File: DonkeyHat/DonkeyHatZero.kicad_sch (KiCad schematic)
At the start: 17 parts, among them J1 GPIO, J2 Encoder 2, J3 Encoder 1, J4 I2C, J5 Battery +, J6 Battery -, J7 +5v, J8 GND, U2 rp2040-zero

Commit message: Zero WIP
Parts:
- removed 5V1: Conn_01x02_Pin, Connector_PinHeader_2.54mm:PinHeader_1x02_P2.54mm_Vertical, symbol Connector:Conn_01x02_Pin
- removed I2C1, OLED1: Conn_01x04_Pin, Connector_PinHeader_2.54mm:PinHeader_1x04_P2.54mm_Vertical, symbol Connector:Conn_01x04_Pin
- removed J2: Encoder 2, Connector_PinHeader_2.54mm:PinHeader_1x04_P2.54mm_Vertical, symbol Connector:Conn_01x04_Pin
- removed J3: Encoder 1, Connector_PinHeader_2.54mm:PinHeader_1x04_P2.54mm_Vertical, symbol Connector:Conn_01x04_Pin
- removed J4: I2C, Connector_JST:JST_SH_BM04B-SRSS-TB_1x04-1MP_P1.00mm_Vertical, symbol dk_Rectangular-Connectors-Headers-Male-Pins:B4B-PH-K-S_LF__SN_
- added J2, J3: Conn_01x02_Pin, Connector_PinHeader_2.54mm:PinHeader_1x02_P2.54mm_Vertical, symbol Connector:Conn_01x02_Pin
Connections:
- net GND: no longer J1.20 (Pin_20), J1.25 (Pin_25), J1.30 (Pin_30), J1.34 (Pin_34), J1.39 (Pin_39), J1.9 (Pin_9)
- net GPIO2/SDA1: no longer J1.3 (Pin_3)
- net GPIO3/SCL1: no longer J1.5 (Pin_5)
- net GPIO5: no longer J1.29 (Pin_29)
- net at J6.1 (Pin_1): now also J2.2 (Pin_2), J3.2 (Pin_2)
- net at J5.1 (Pin_1): now also J2.1 (Pin_1), J3.1 (Pin_1)
- net +3V3: no longer names the net of J1.1 (Pin_1)
- net +3V3: no longer J1.17 (Pin_17)
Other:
- moved on the sheet: J5, J6

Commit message: Ready for routing
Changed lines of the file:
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@@
 	(wire
 		(pts
-			(xy 121.92 29.21) (xy 133.35 29.21)
+			(xy 121.92 29.21) (xy 139.7 29.21)
 		)
 		(stroke
@@
 	(wire
 		(pts
-			(xy 133.35 29.21) (xy 133.35 43.18)
+			(xy 139.7 29.21) (xy 139.7 43.18)
 		)
 		(stroke
@@
 	(wire
 		(pts
-			(xy 116.84 43.18) (xy 133.35 43.18)
+			(xy 116.84 43.18) (xy 139.7 43.18)
 		)
 		(stroke
@@
 					(unit 1)
 				)
+			)
+		)
+	)
+	(symbol
+		(lib_id "power:GND")
+		(at 127 35.56 90)
+		(unit 1)
+		(exclude_from_sim no)
+		(in_bom yes)
+		(on_board yes)
+		(dnp no)
+		(property "Reference" "#PWR07"
+			(at 133.35 35.56 0)
+			(effects
+				(font
+					(size 1.27 1.27)
+				)
+				(hide yes)
+			)
+		)
+		(property "Value" "GND"
+			(at 131.3244 35.4457 0)
+			(effects
+				(font
+					(size 1.27 1.27)
+				)
+			)
+		)
+		(property "Footprint" ""
+			(at 127 35.56 0)
+			(effects
+				(font
+					(size 1.27 1.27)
+				)
+			)
+		)
+		(property "Datasheet" ""
+			(at 127 35.56 0)
+			(effects
+				(font
+					(size 1.27 1.27)
+				)
+			)
+		)
+		(property "Description" ""
+			(at 127 35.56 0)
+			(effects
+				(font
+					(size 1.27 1.27)
+				)
+				(hide yes)
+			)
+		)
+		(pin "1"
+		)
+		(instances
+			(project "DonkeyHatZero"
+				(path "/e63e39d7-6ac0-4ffd-8aa3-1841a4541b55"
+					(reference "#PWR07")
+					(unit 1)
+				)

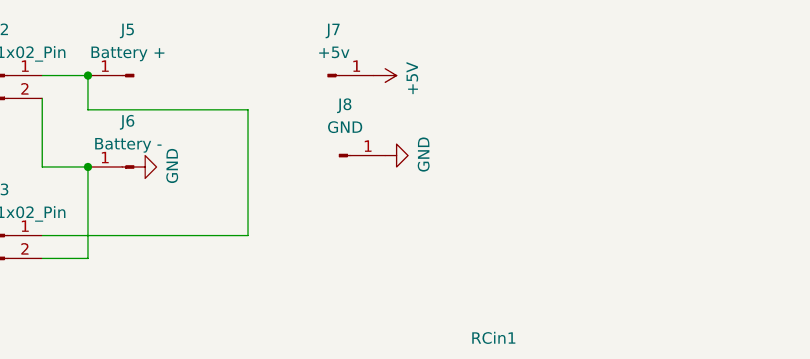
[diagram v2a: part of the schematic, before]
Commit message: Fixed spacing
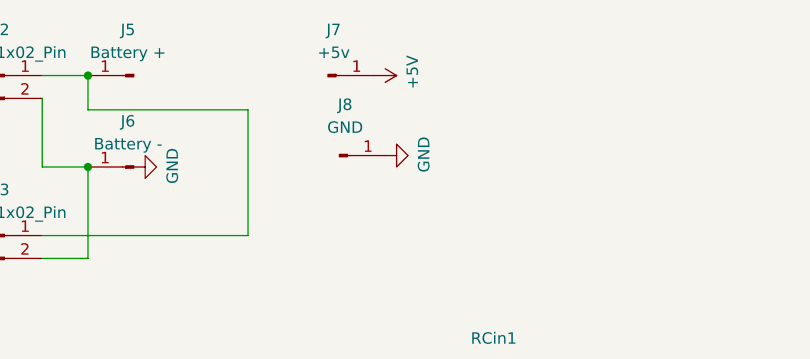
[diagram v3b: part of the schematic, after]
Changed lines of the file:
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@@
+	)
+	(symbol
+		(lib_id "power:+5V")
+		(at 153.67 25.4 270)
+		(mirror x)
+		(unit 1)
+		(exclude_from_sim no)
+		(in_bom yes)
+		(on_board yes)
+		(dnp no)
+		(property "Reference" "#PWR09"
+			(at 149.86 25.4 0)
+			(effects
+				(font
+					(size 1.27 1.27)
+				)
+				(hide yes)
+			)
+		)
+		(property "Value" "+5V"
+			(at 157.9944 25.0317 0)
+			(effects
+				(font
+					(size 1.27 1.27)
+				)
+			)
+		)
+		(property "Footprint" ""
+			(at 153.67 25.4 0)
+			(effects
+				(font
+					(size 1.27 1.27)
+				)
+			)
+		)
+		(property "Datasheet" ""
+			(at 153.67 25.4 0)
+			(effects
+				(font
+					(size 1.27 1.27)
+				)
+			)
+		)
+		(property "Description" ""
+			(at 153.67 25.4 0)
+			(effects
+				(font
+					(size 1.27 1.27)
+				)
+				(hide yes)
+			)
+		)
+		(pin "1"
+		)
+		(instances
+			(project "DonkeyHatZero"
+				(path "/e63e39d7-6ac0-4ffd-8aa3-1841a4541b55"
+					(reference "#PWR09")
+					(unit 1)
+				)
+			)
+		)
 	)
 	(symbol
@@
 					(unit 1)
 				)
-			)
-		)
-	)
-	(symbol
-		(lib_id "power:+5V")
-		(at 153.67 25.4 270)
-		(unit 1)
-		(exclude_from_sim no)
-		(in_bom yes)
-		(on_board yes)
-		(dnp no)
-		(property "Reference" "#PWR013"
-			(at 149.86 25.4 0)
-			(effects
-				(font
-					(size 1.27 1.27)
-				)
-				(hide yes)
-			)
-		)
-		(property "Value" "+5V"
-			(at 157.9944 25.7683 0)
-			(effects
-				(font
-					(size 1.27 1.27)
-				)
-			)
-		)
-		(property "Footprint" ""
-			(at 153.67 25.4 0)
-			(effects
-				(font
-					(size 1.27 1.27)
-				)
-			)
-		)
-		(property "Datasheet" ""
-			(at 153.67 25.4 0)
-			(effects
-				(font
-					(size 1.27 1.27)
-				)
-			)
-		)
-		(property "Description" ""
-			(at 153.67 25.4 0)
-			(effects
-				(font
-					(size 1.27 1.27)
-				)
-				(hide yes)
-			)
-		)
-		(pin "1"
-		)
-		(instances
-			(project "DonkeyHatZero"
-				(path "/e63e39d7-6ac0-4ffd-8aa3-1841a4541b55"
-					(reference "#PWR013")
-					(unit 1)
-				)

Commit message: Updated zero
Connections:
- net GND: now also J3.1 (Pin_1)
- net at J2.2 (Pin_2), J6.1 (Pin_1): no longer J3.2 (Pin_2)
- net at J2.1 (Pin_1), J5.1 (Pin_1): now also J3.2 (Pin_2); no longer J3.1 (Pin_1)
- net Batt: no longer names the net of RCin1.2 (Pin_2), Steer1.2 (Pin_2)
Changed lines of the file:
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@@
-	)
-	(junction
-		(at 121.92 35.56)
-		(diameter 0)
-		(color 0 0 0 0)
 	)
 	(junction
@@
 	(wire
 		(pts
-			(xy 154.94 62.23) (xy 162.56 62.23)
-		)
-		(stroke
-			(width 0)
-			(type default)
-		)
-	)
-	(wire
-		(pts
 			(xy 218.44 87.63) (xy 224.79 87.63)
 		)
@@
 	(wire
 		(pts
+			(xy 151.13 62.23) (xy 162.56 62.23)
+		)
+		(stroke
+			(width 0)
+			(type default)
+		)
+	)
+	(wire
+		(pts
+			(xy 139.7 45.72) (xy 116.84 45.72)
+		)
+		(stroke
+			(width 0)
+			(type default)
+		)
+	)
+	(wire
+		(pts
 			(xy 85.09 24.13) (xy 96.52 24.13)
 		)
@@
 	(wire
 		(pts
-			(xy 121.92 35.56) (xy 121.92 45.72)
-		)
-		(stroke
-			(width 0)
-			(type default)
-		)
-	)
-	(wire
-		(pts
 			(xy 200.66 93.98) (xy 199.39 93.98)
 		)
@@
 	(wire
 		(pts
-			(xy 154.94 83.82) (xy 162.56 83.82)
-		)
-		(stroke
-			(width 0)
-			(type default)
-		)
-	)
-	(wire
-		(pts
 			(xy 31.75 35.56) (xy 60.96 35.56)
 		)
@@
 	(wire
 		(pts
+			(xy 116.84 43.18) (xy 123.19 43.18)
+		)
+		(stroke
+			(width 0)
+			(type default)
+		)
+	)
+	(wire
+		(pts
+			(xy 151.13 62.23) (xy 151.13 83.82)
+		)
+		(stroke
+			(width 0)
+			(type default)
+		)
+	)
+	(wire
+		(pts
 			(xy 31.75 45.72) (xy 60.96 45.72)
 		)
@@
 	(wire
 		(pts
-			(xy 139.7 29.21) (xy 139.7 43.18)
-		)
-		(stroke
-			(width 0)
-			(type default)
-		)
-	)
-	(wire
-		(pts
-			(xy 121.92 45.72) (xy 116.84 45.72)
+			(xy 139.7 29.21) (xy 139.7 45.72)
 		)
 		(stroke
@@
 	(wire
 		(pts
-			(xy 116.84 43.18) (xy 139.7 43.18)
-		)
-		(stroke
-			(width 0)
-			(type default)
-		)
-	)
-	(wire
-		(pts
 			(xy 200.66 92.71) (xy 200.66 93.98)
 		)
@@
 	(wire
 		(pts
+			(xy 123.19 35.56) (xy 127 35.56)
+		)
+		(stroke
+			(width 0)
+			(type default)
+		)
+	)
+	(wire
+		(pts
+			(xy 151.13 83.82) (xy 162.56 83.82)
+		)
+		(stroke
+			(width 0)
+			(type default)
+		)
+	)
+	(wire
+		(pts
 			(xy 73.66 38.1) (xy 90.17 38.1)
+		)
+		(stroke
+			(width 0)
+			(type default)
+		)
+	)
+	(wire
+		(pts
+			(xy 123.19 43.18) (xy 123.19 35.56)
 		)
 		(stroke
@@
 					(unit 1)
 				)
-			)
-		)
-	)
-	(symbol
-		(lib_id "power:+5V")
-		(at 154.94 62.23 90)
-		(unit 1)
-		(exclude_from_sim no)
-		(in_bom yes)
-		(on_board yes)
-		(dnp no)
-		(property "Reference" "#PWR16"
-			(at 158.75 62.23 0)
-			(effects
-				(font
-					(size 1.27 1.27)
-				)
-				(hide yes)
-			)
-		)
-		(property "Value" "Batt"
-			(at 150.6156 61.8617 0)
-			(effects
-				(font
-					(size 1.27 1.27)
-				)
-			)
-		)
-		(property "Footprint" ""
-			(at 154.94 62.23 0)
-			(effects
-				(font
-					(size 1.27 1.27)
-				)
-			)
-		)
-		(property "Datasheet" ""
-			(at 154.94 62.23 0)
-			(effects
-				(font
-					(size 1.27 1.27)
-				)
-			)
-		)
-		(property "Description" ""
-			(at 154.94 62.23 0)
-			(effects
-				(font
-					(size 1.27 1.27)
-				)
-				(hide yes)
-			)
-		)
-		(pin "1"
-		)
-		(instances
-			(project "DonkeyHat"
-				(path "/e63e39d7-6ac0-4ffd-8aa3-1841a4541b55"
-					(reference "#PWR16")
-					(unit 1)
-				)
-			)
-		)
-	)
-	(symbol
-		(lib_id "power:+5V")
-		(at 154.94 83.82 90)
-		(unit 1)
-		(exclude_from_sim no)
-		(in_bom yes)
-		(on_board yes)
-		(dnp no)
-		(property "Reference" "#PWR08"
-			(at 158.75 83.82 0)
-			(effects
-				(font
-					(size 1.27 1.27)
-				)
-				(hide yes)
-			)
-		)
-		(property "Value" "Batt"
-			(at 150.6156 83.4517 0)
-			(effects
-				(font
-					(size 1.27 1.27)
-				)
-			)
-		)
-		(property "Footprint" ""
-			(at 154.94 83.82 0)
-			(effects
-				(font
-					(size 1.27 1.27)
-				)
-			)
-		)
-		(property "Datasheet" ""
-			(at 154.94 83.82 0)
-			(effects
-				(font
-					(size 1.27 1.27)
-				)
-			)
-		)
-		(property "Description" ""
-			(at 154.94 83.82 0)
-			(effects
-				(font
-					(size 1.27 1.27)
-				)
-				(hide yes)
-			)
-		)
-		(pin "1"
-		)
-		(instances
-			(project "DonkeyHatZero"
-				(path "/e63e39d7-6ac0-4ffd-8aa3-1841a4541b55"
-					(reference "#PWR08")
-					(unit 1)
-				)
